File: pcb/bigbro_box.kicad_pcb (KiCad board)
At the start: 2 copper layers, 100 x 58 mm, 48 parts, among them J1 Current Sense, J2 Display, J3 Mains, J4 Debug, J5 RFID, J6 Relay, J7 Ext, K1 G5LE-1, Q1 MMBT3904, Q2 MMBT3904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

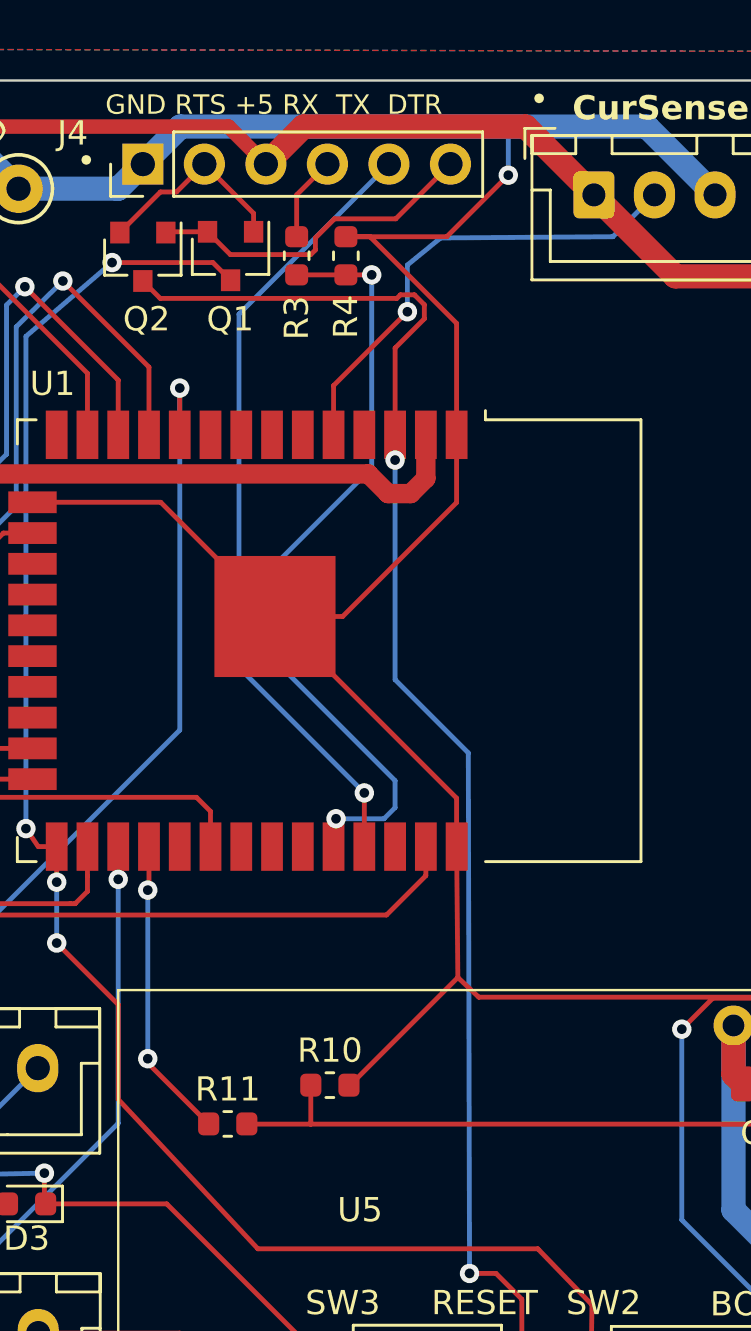
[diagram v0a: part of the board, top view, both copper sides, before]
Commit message: Add RTS pullup.
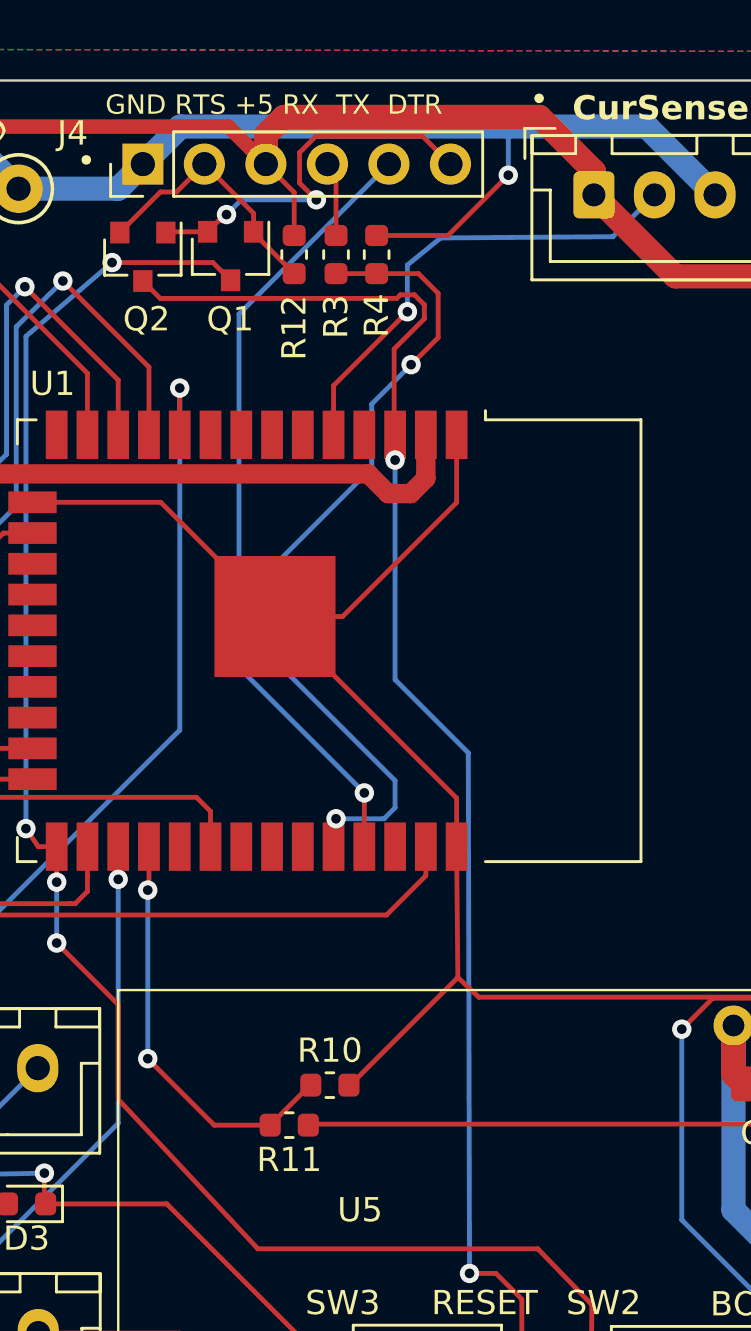
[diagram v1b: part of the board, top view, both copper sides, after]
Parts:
- added R12: 4k7, Resistor_SMD:R_0603_1608Metric, F.Cu at (135.0, 64.2)
- C1: value 1uF -> 1u
- C2: value 10uF -> 10u
- R1: value 1k -> 4k7
- R2: value 10k -> 1k
- moved R11 2.54 mm to (134.8, 100.1), turned to 180 degrees
- moved R3 1.63 mm to (136.8, 64.2)
- moved R4 1.27 mm to (138.4, 64.2)
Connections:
- net /~{RTS} renamed ~{RTS}
- R10 pad 1: Net-(U5-TX) -> ESP_RFID_TX
- R11 pad 1: ESP_RFID_TX -> Net-(U5-TX)
- R11 pad 2: Net-(U5-TX) -> ESP_RFID_TX
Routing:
- net GND: track 311.1 -> 299.1 mm
- net +5V: track 197.3 -> 202.3 mm
- net ESP_RFID_TX: track 12.5 -> 17.5 mm
- net Net-(U5-TX): track 33.6 -> 29.3 mm
- net ~{RTS}: track 8.30 -> 10.7 mm
- net /~{DTR}: track 14.0 -> 16.0 mm, vias 0 -> 2
- net /MCU_RX0: track 33.5 -> 35.4 mm

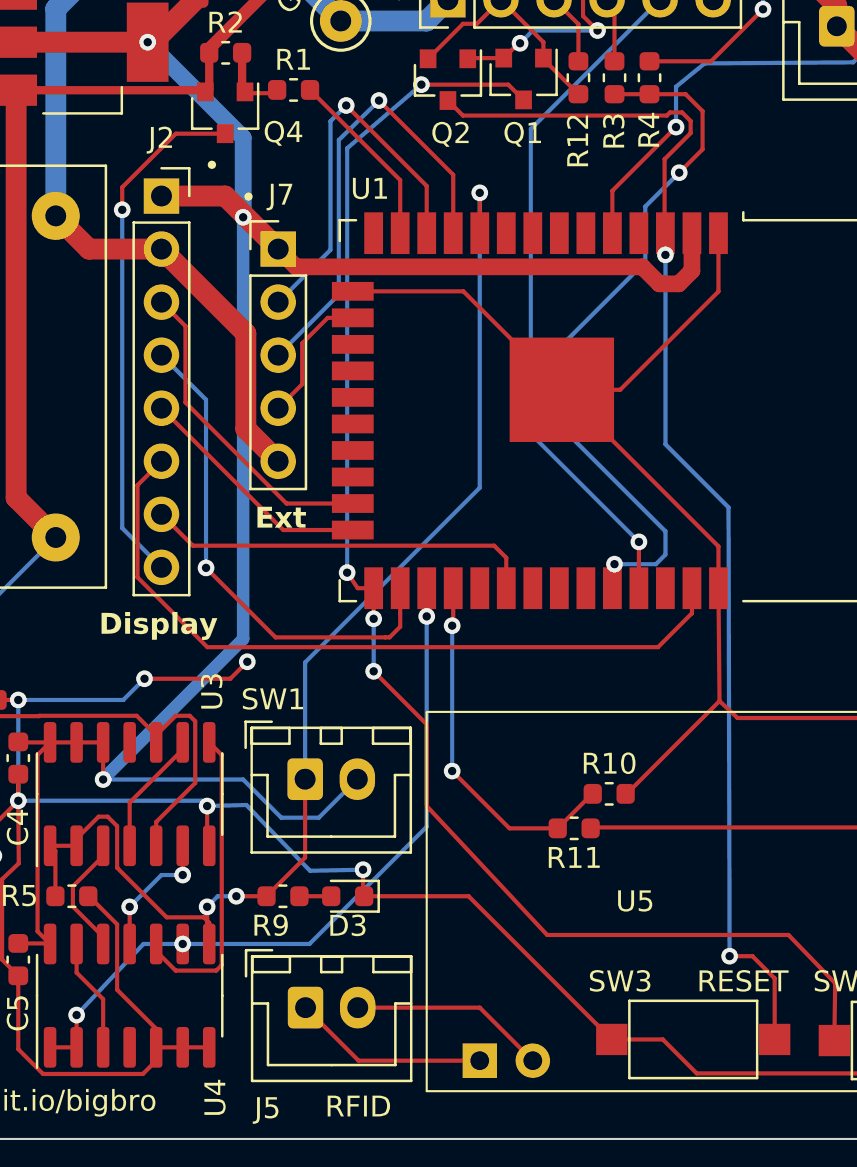
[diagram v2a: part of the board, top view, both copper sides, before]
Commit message: Add C6.
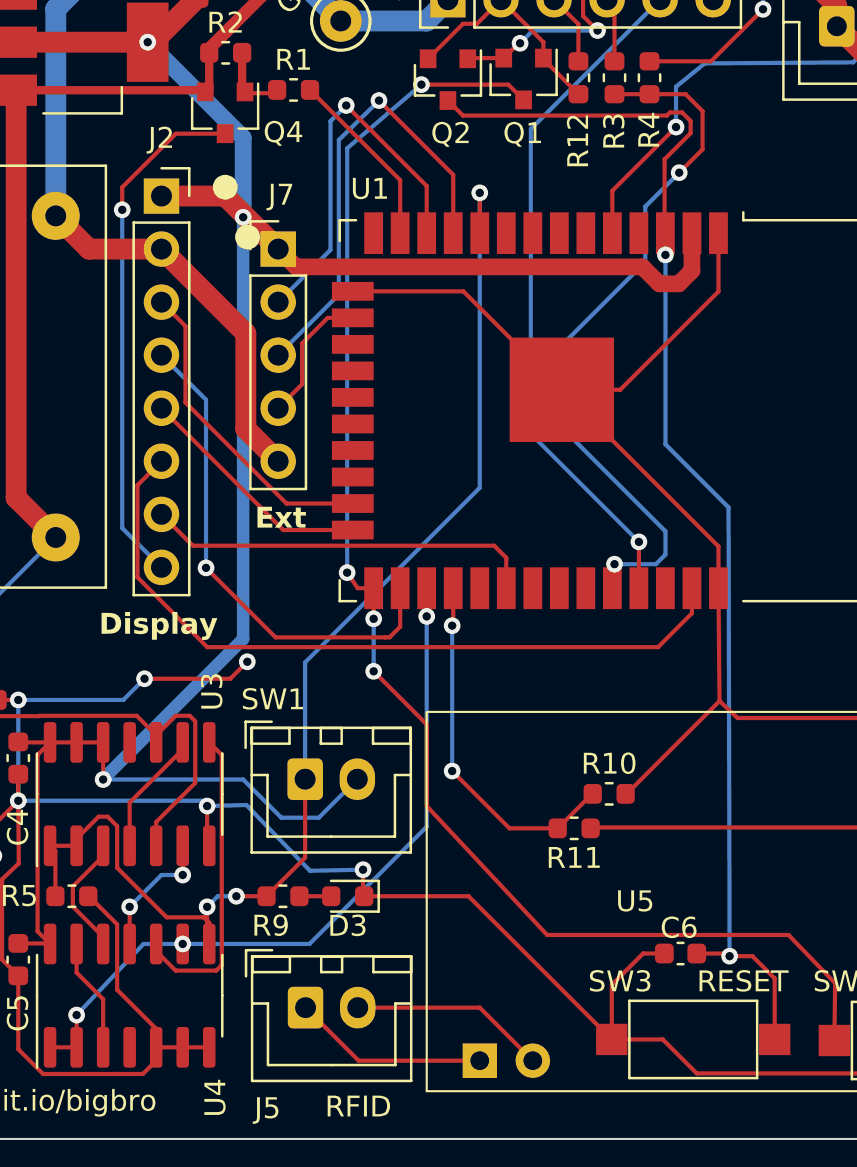
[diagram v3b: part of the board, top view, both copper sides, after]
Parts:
- added C6: 100n, Capacitor_SMD:C_0603_1608Metric, F.Cu at (139.9, 106.1)
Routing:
- net GND: track 299.1 -> 304.9 mm
- net /~{RESET}: track 59.4 -> 61.1 mm

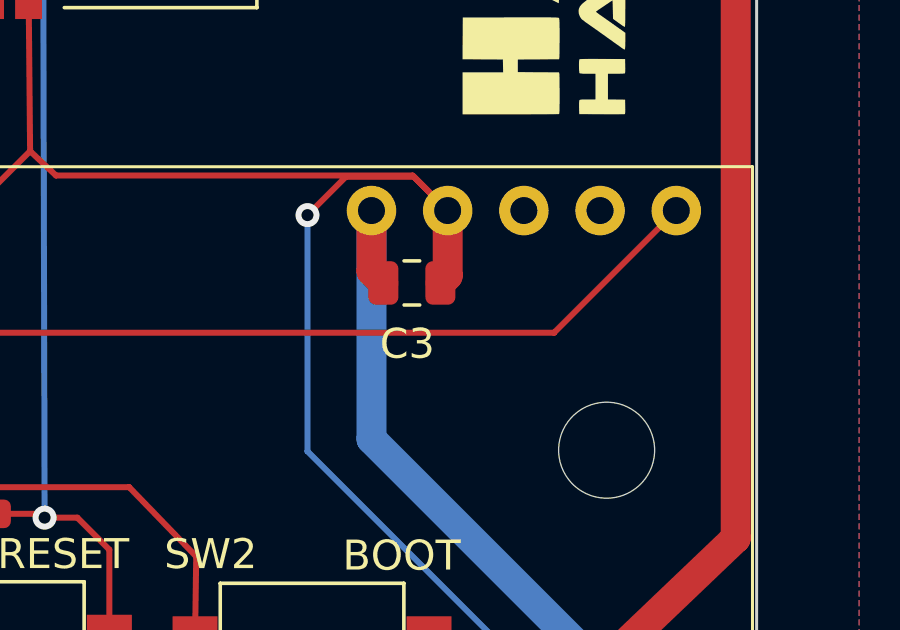
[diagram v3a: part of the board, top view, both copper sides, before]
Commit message: Change C3 to 0608.
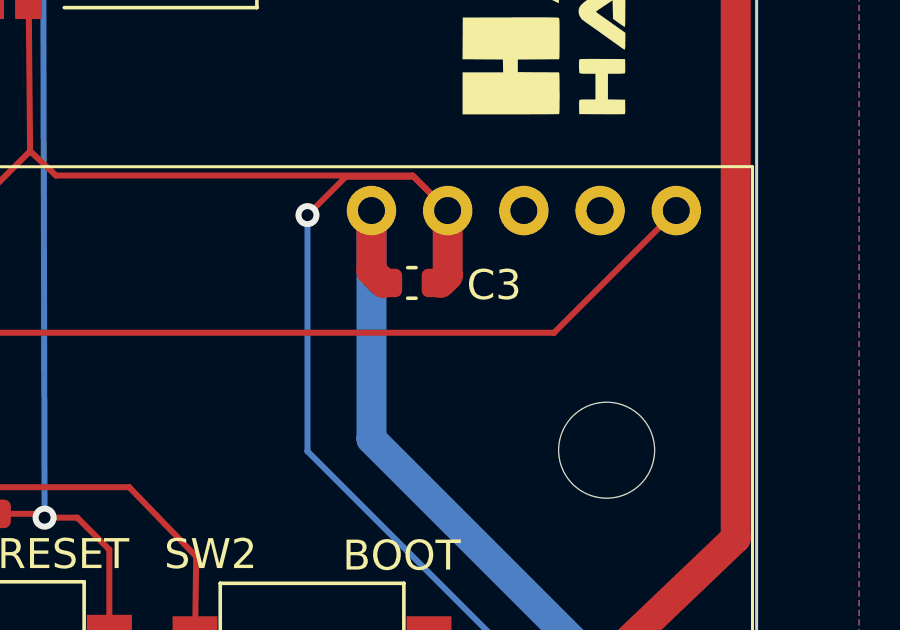
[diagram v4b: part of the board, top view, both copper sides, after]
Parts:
- C3: footprint Capacitor_SMD:C_0805_2012Metric -> Capacitor_SMD:C_0603_1608Metric
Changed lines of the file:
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@@
 (kicad_pcb
-	(version 20241010)
+	(version 20241030)
 	(generator "pcbnew")
 	(generator_version "8.99")
@@
 		(tags "capacitor")
 		(property "Reference" "C6"
-			(at 0.0638 1.2192 360)
+			(at 0.0638 1.2192 0)
 			(layer "F.SilkS")
 			(effects
@@
 		)
 		(property "Value" "100n"
-			(at 0 1.43 360)
+			(at 0 1.43 0)
 			(layer "F.Fab")
 			(effects
@@
 		)
 		(property "Footprint" "Capacitor_SMD:C_0603_1608Metric"
-			(at 0 0 360)
+			(at 0 0 0)
 			(layer "F.Fab")
 			(hide yes)
@@
 		)
 		(property "Datasheet" ""
-			(at 0 0 360)
+			(at 0 0 0)
 			(layer "F.Fab")
 			(hide yes)
@@
 		)
 		(property "Description" "Unpolarized capacitor"
-			(at 0 0 360)
+			(at 0 0 0)
 			(layer "F.Fab")
 			(hide yes)
@@
 		)
 		(fp_text user "${REFERENCE}"
-			(at 0 0 360)
+			(at 0 0 0)
 			(layer "F.Fab")
 			(effects
@@
 		)
 	)
-	(footprint "Capacitor_SMD:C_0805_2012Metric"
+	(footprint "Capacitor_SMD:C_0603_1608Metric"
 		(layer "F.Cu")
 		(at 154.5082 98.425)
-		(descr "Capacitor SMD 0805 (2012 Metric), square (rectangular) end terminal, IPC_7351 nominal, (Body size source: IPC-SM-782 page 76, https://www.pcb-3d.com/wordpress/wp-content/uploads/ipc-sm-782a_amendment_1_and_2.pdf, https://docs.google.com/spreadsheets/d/1BsfQQcO9C6DZCsRaXUlFlo91Tg2WpOkGARC1WS5S8t0/edit?usp=sharing), generated with kicad-footprint-generator")
+		(descr "Capacitor SMD 0603 (1608 Metric), square (rectangular) end terminal, IPC_7351 nominal, (Body size source: IPC-SM-782 page 76, https://www.pcb-3d.com/wordpress/wp-content/uploads/ipc-sm-782a_amendment_1_and_2.pdf), generated with kicad-footprint-generator")
 		(tags "capacitor")
 		(property "Reference" "C3"
-			(at -0.1524 2.032 0)
+			(at 2.7418 0.075 0)
 			(layer "F.SilkS")
 			(effects
@@
 		)
 		(property "Value" "10u"
-			(at 0 1.68 0)
+			(at 0 1.43 0)
 			(layer "F.Fab")
 			(effects
@@
 			)
 		)
-		(property "Footprint" "Capacitor_SMD:C_0805_2012Metric"
+		(property "Footprint" "Capacitor_SMD:C_0603_1608Metric"
 			(at 0 0 0)
-			(unlocked yes)
 			(layer "F.Fab")
 			(hide yes)
@@
 		(property "Datasheet" ""
 			(at 0 0 0)
-			(unlocked yes)
 			(layer "F.Fab")
 			(hide yes)
@@
 		(property "Description" ""
 			(at 0 0 0)
-			(unlocked yes)
 			(layer "F.Fab")
 			(hide yes)
@@
 		(attr smd)
 		(fp_line
-			(start -0.261252 -0.735)
-			(end 0.261252 -0.735)
+			(start -0.14058 -0.51)
+			(end 0.14058 -0.51)
 			(stroke
 				(width 0.12)
@@
 		)
 		(fp_line
-			(start -0.261252 0.735)
-			(end 0.261252 0.735)
+			(start -0.14058 0.51)
+			(end 0.14058 0.51)
 			(stroke
 				(width 0.12)
@@
 		)
 		(fp_line
-			(start -1.7 -0.98)
-			(end 1.7 -0.98)
+			(start -1.48 -0.73)
+			(end 1.48 -0.73)
 			(stroke
 				(width 0.05)
@@
 		)
 		(fp_line
-			(start -1.7 0.98)
-			(end -1.7 -0.98)
+			(start -1.48 0.73)
+			(end -1.48 -0.73)
 			(stroke
 				(width 0.05)
@@
 		)
 		(fp_line
-			(start 1.7 -0.98)
-			(end 1.7 0.98)
+			(start 1.48 -0.73)
+			(end 1.48 0.73)
 			(stroke
 				(width 0.05)
@@
 		)
 		(fp_line
-			(start 1.7 0.98)
-			(end -1.7 0.98)
+			(start 1.48 0.73)
+			(end -1.48 0.73)
 			(stroke
 				(width 0.05)
@@
 		)
 		(fp_line
-			(start -1 -0.625)
-			(end 1 -0.625)
+			(start -0.8 -0.4)
+			(end 0.8 -0.4)
 			(stroke
 				(width 0.1)
@@
 		)
 		(fp_line
-			(start -1 0.625)
-			(end -1 -0.625)
+			(start -0.8 0.4)
+			(end -0.8 -0.4)
 			(stroke
 				(width 0.1)
@@
 		)
 		(fp_line
-			(start 1 -0.625)
-			(end 1 0.625)
+			(start 0.8 -0.4)
+			(end 0.8 0.4)
 			(stroke
 				(width 0.1)
@@
 		)
 		(fp_line
-			(start 1 0.625)
-			(end -1 0.625)
+			(start 0.8 0.4)
+			(end -0.8 0.4)
 			(stroke
 				(width 0.1)
@@
 			(effects
 				(font
-					(size 0.5 0.5)
-					(thickness 0.08)
+					(size 0.4 0.4)
+					(thickness 0.06)
 				)
 			)
 		)
 		(pad "1" smd roundrect
-			(at -0.95 0)
-			(size 1 1.45)
+			(at -0.775 0)
+			(size 0.9 0.95)
 			(layers "F.Cu" "F.Mask" "F.Paste")
 			(roundrect_rratio 0.25)
@@
 		)
 		(pad "2" smd roundrect
-			(at 0.95 0)
-			(size 1 1.45)
+			(at 0.775 0)
+			(size 0.9 0.95)
 			(layers "F.Cu" "F.Mask" "F.Paste")
 			(roundrect_rratio 0.25)
@@
 		)
 		(embedded_fonts no)
-		(model "${KICAD6_3DMODEL_DIR}/Capacitor_SMD.3dshapes/C_0805_2012Metric.wrl"
+		(model "${KICAD6_3DMODEL_DIR}/Capacitor_SMD.3dshapes/C_0603_1608Metric.wrl"
 			(offset
 				(xyz 0 0 0)
@@
 			(footprints allowed)
 		)
+		(placement
+			(enabled no)
+			(sheetname "")
+		)
 		(fill
 			(thermal_gap 0.5)
@@
 			(footprints allowed)
 		)
+		(placement
+			(enabled no)
+			(sheetname "")
+		)
 		(fill
 			(thermal_gap 0.5)
@@
 			(footprints allowed)
 		)
+		(placement
+			(enabled no)
+			(sheetname "")
+		)
 		(fill

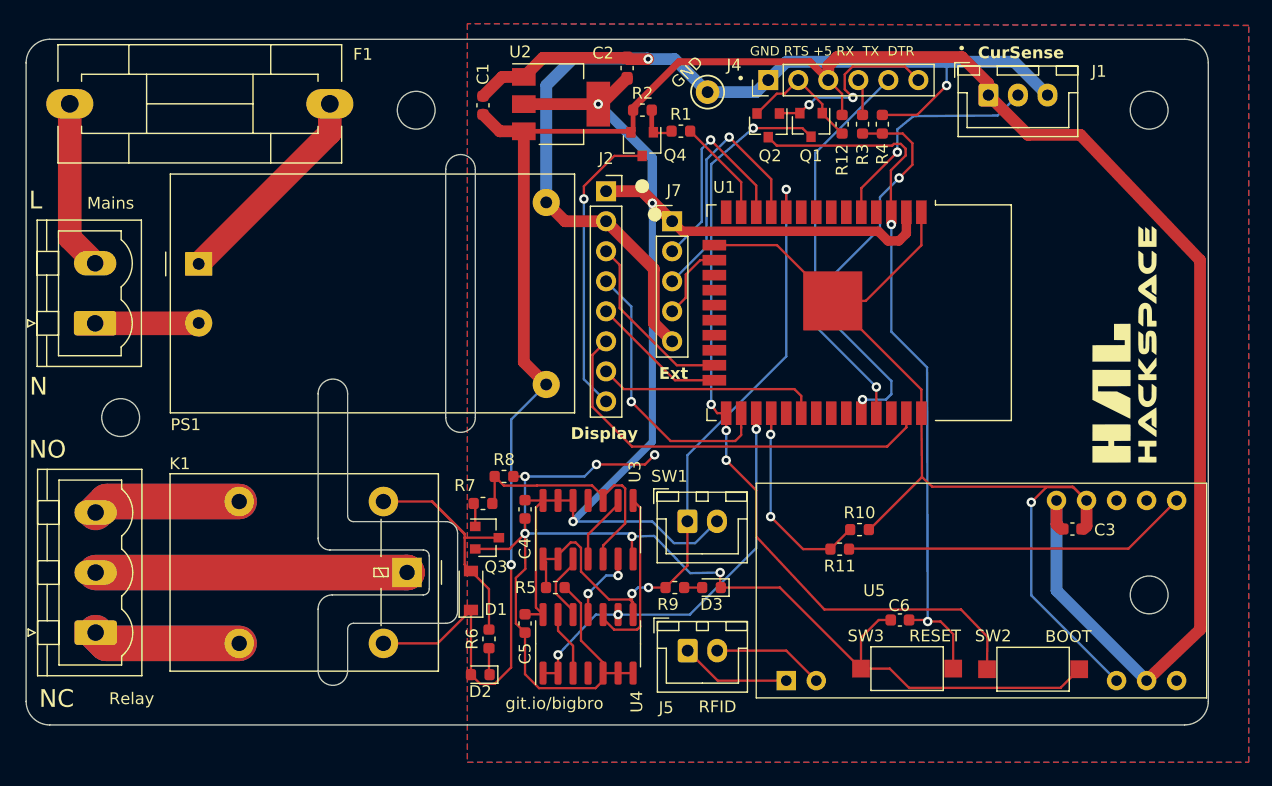
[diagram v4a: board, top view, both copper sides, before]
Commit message: Add thermal pad.
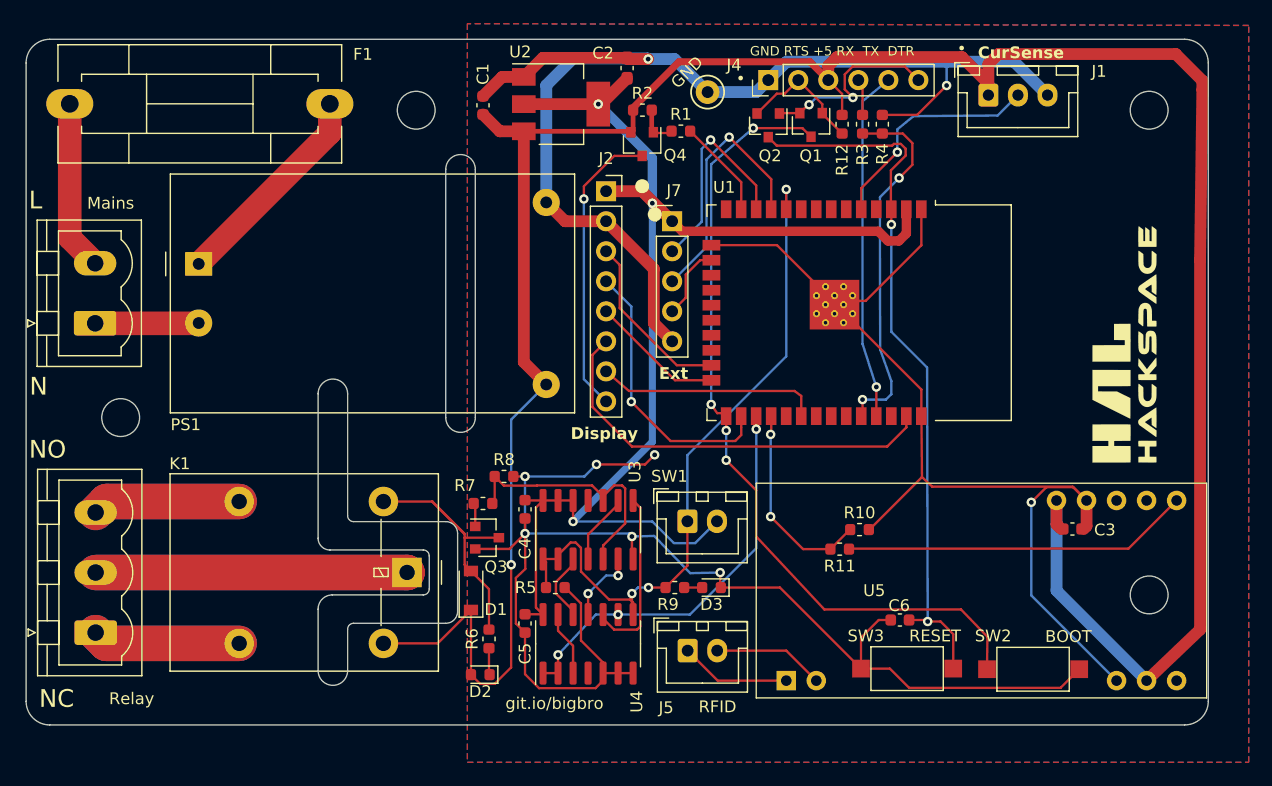
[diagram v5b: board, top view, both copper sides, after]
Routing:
- net +5V: track 202.3 -> 215.7 mm
- net /MCU_RX0: track 35.4 -> 30.9 mm
- net /MCU_TX0: track 32.9 -> 29.4 mm
